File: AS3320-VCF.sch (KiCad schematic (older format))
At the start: 41 parts, among them J5 SIGNAL_INPUT, U1 AS3320

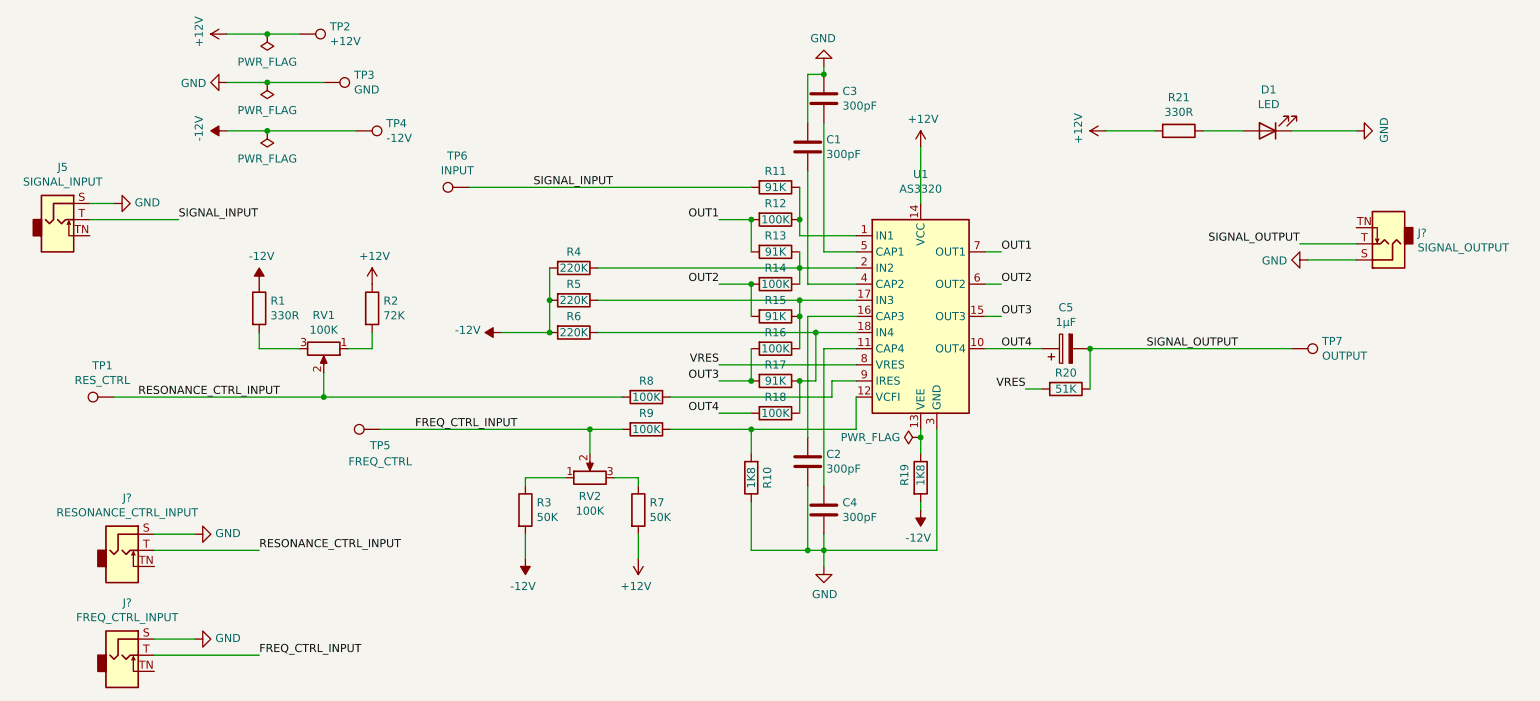
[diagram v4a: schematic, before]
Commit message: Reroute tracks.
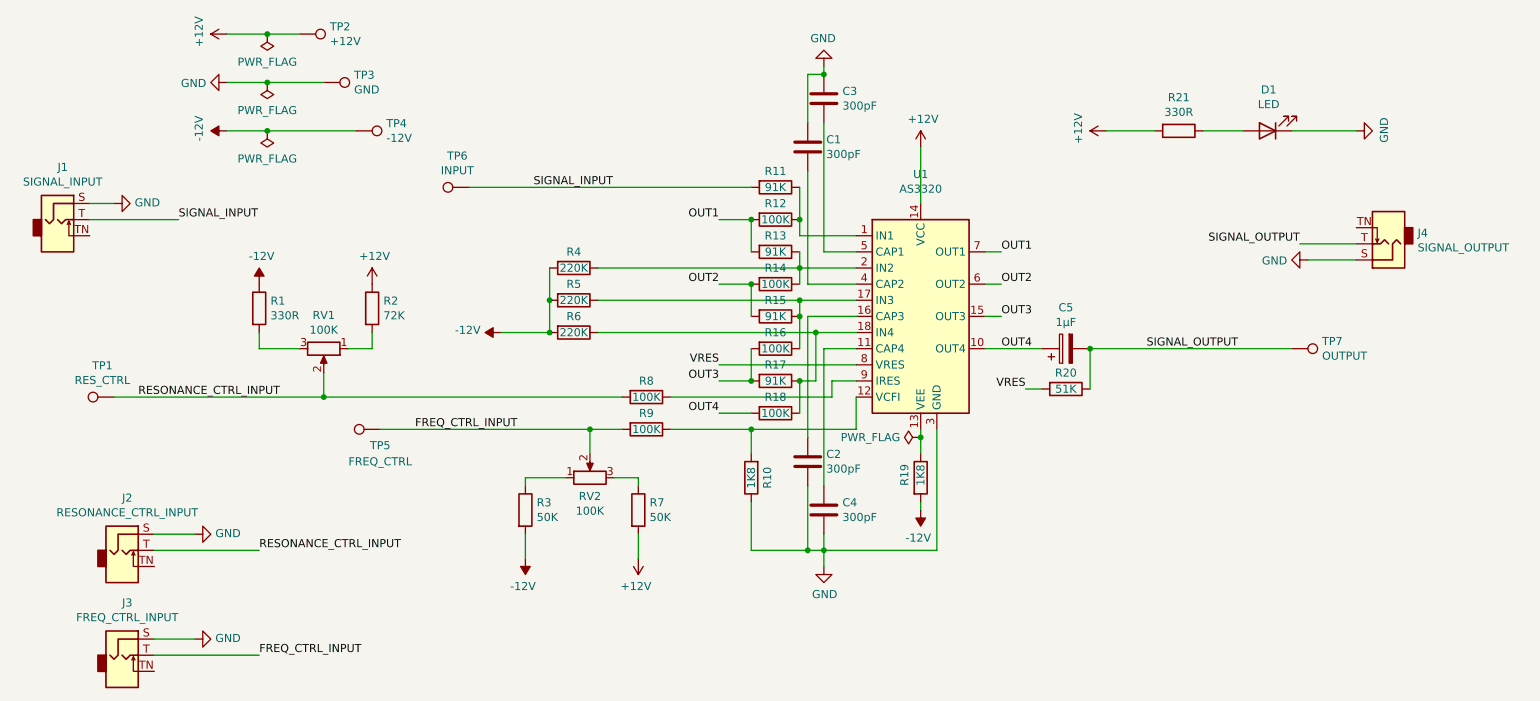
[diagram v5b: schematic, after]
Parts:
- gave numbers to parts that had none: 3
- renumbered J5 to J1
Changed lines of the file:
@@
 	8850 3400 9150 3400
 $Comp
-L power:GND #PWR016
+L power:GND #PWR017
 U 1 1 5F823993
 P 8850 3400
-F 0 "#PWR016" H 8850 3150 50  0001 C CNN
+F 0 "#PWR017" H 8850 3150 50  0001 C CNN
 F 1 "GND" V 8855 3272 50  0000 R CNN
 F 2 "" H 8850 3400 50  0001 C CNN
@@
 $EndComp
 $Comp
-L power:+12V #PWR0101
+L power:+12V #PWR016
 U 1 1 5F9C478A
 P 7600 2600
-F 0 "#PWR0101" H 7600 2450 50  0001 C CNN
+F 0 "#PWR016" H 7600 2450 50  0001 C CNN
 F 1 "+12V" H 7615 2773 50  0000 C CNN
 F 2 "" H 7600 2600 50  0001 C CNN
@@
 	8200 2600 8450 2600
 $Comp
-L power:GND #PWR0102
+L power:GND #PWR018
 U 1 1 5F9D4349
 P 9150 2600
-F 0 "#PWR0102" H 9150 2350 50  0001 C CNN
+F 0 "#PWR018" H 9150 2350 50  0001 C CNN
 F 1 "GND" H 9155 2427 50  0000 C CNN
 F 2 "" H 9150 2600 50  0001 C CNN
@@
 Connection ~ 2400 2000
 $Comp
-L power:PWR_FLAG #FLG0101
+L power:PWR_FLAG #FLG01
 U 1 1 5F973F3F
 P 2400 2000
-F 0 "#FLG0101" H 2400 2075 50  0001 C CNN
+F 0 "#FLG01" H 2400 2075 50  0001 C CNN
 F 1 "PWR_FLAG" H 2400 2173 50  0000 C CNN
 F 2 "" H 2400 2000 50  0001 C CNN
@@
 Connection ~ 2400 2600
 $Comp
-L power:PWR_FLAG #FLG0102
+L power:PWR_FLAG #FLG03
 U 1 1 5F97BA16
 P 2400 2600
-F 0 "#FLG0102" H 2400 2675 50  0001 C CNN
+F 0 "#FLG03" H 2400 2675 50  0001 C CNN
 F 1 "PWR_FLAG" H 2400 2773 50  0000 C CNN
 F 2 "" H 2400 2600 50  0001 C CNN
@@
 	2150 2300 2400 2300
 $Comp
-L power:PWR_FLAG #FLG0104
+L power:PWR_FLAG #FLG02
 U 1 1 5F9E0E08
 P 2400 2300
-F 0 "#FLG0104" H 2400 2375 50  0001 C CNN
+F 0 "#FLG02" H 2400 2375 50  0001 C CNN
 F 1 "PWR_FLAG" H 2400 2473 50  0000 C CNN
 F 2 "" H 2400 2300 50  0001 C CNN
@@
 	6450 4450 6450 4500
 $Comp
-L power:PWR_FLAG #FLG0103
+L power:PWR_FLAG #FLG04
 U 1 1 5F9E8A50
 P 6450 4500
-F 0 "#FLG0103" H 6450 4575 50  0001 C CNN
+F 0 "#FLG04" H 6450 4575 50  0001 C CNN
 F 1 "PWR_FLAG" V 6450 4627 50  0000 L CNN
 F 2 "" H 6450 4500 50  0001 C CNN
@@
 	6450 4500 6450 4600
 $Comp
-L Connector:AudioJack2_SwitchT J5
+L Connector:AudioJack2_SwitchT J1
 U 1 1 5F9F3358
 P 1100 3150
-F 0 "J5" H 1132 3475 50  0000 C CNN
+F 0 "J1" H 1132 3475 50  0000 C CNN
 F 1 "SIGNAL_INPUT" H 1132 3384 50  0000 C CNN
 F 2 "SeattleSynths:Jack_3.5mm_QingPu_WQP-PJ398SM_Vertical_CircularHoles" H 1100 3150 50  0001 C CNN
@@
 SIGNAL_INPUT
 $Comp
-L Connector:AudioJack2_SwitchT J?
+L Connector:AudioJack2_SwitchT J2
 U 1 1 5FA3B8F2
 P 1500 5200
-F 0 "J?" H 1532 5525 50  0000 C CNN
+F 0 "J2" H 1532 5525 50  0000 C CNN
 F 1 "RESONANCE_CTRL_INPUT" H 1532 5434 50  0000 C CNN
 F 2 "SeattleSynths:Jack_3.5mm_QingPu_WQP-PJ398SM_Vertical_CircularHoles" H 1500 5200 50  0001 C CNN
@@
 $EndComp
 $Comp
-L Connector:AudioJack2_SwitchT J?
+L Connector:AudioJack2_SwitchT J3
 U 1 1 5FA4A748
 P 1500 5850
-F 0 "J?" H 1532 6175 50  0000 C CNN
+F 0 "J3" H 1532 6175 50  0000 C CNN
 F 1 "FREQ_CTRL_INPUT" H 1532 6084 50  0000 C CNN
 F 2 "SeattleSynths:Jack_3.5mm_QingPu_WQP-PJ398SM_Vertical_CircularHoles" H 1500 5850 50  0001 C CNN
@@
 $EndComp
 $Comp
-L Connector:AudioJack2_SwitchT J?
+L Connector:AudioJack2_SwitchT J4
 U 1 1 5FA52FF0
 P 9350 3300
-F 0 "J?" H 9170 3233 50  0000 R CNN
+F 0 "J4" H 9170 3233 50  0000 R CNN
 F 1 "SIGNAL_OUTPUT" H 9170 3324 50  0000 R CNN
 F 2 "SeattleSynths:Jack_3.5mm_QingPu_WQP-PJ398SM_Vertical_CircularHoles" H 9350 3300 50  0001 C CNN
